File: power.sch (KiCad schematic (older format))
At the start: 50 parts, among them CN8 POWER, U1 68000D, U10 74LS244, U11 74LS373, U12 74LS244, U13 74LS373, U2 FAT_AGNUS_8375, U32 74LS139, U34 74LS373, U35 74LS244, U36 74LS05, U37 74LS32, U5 GARY_5719, X1 XTAL

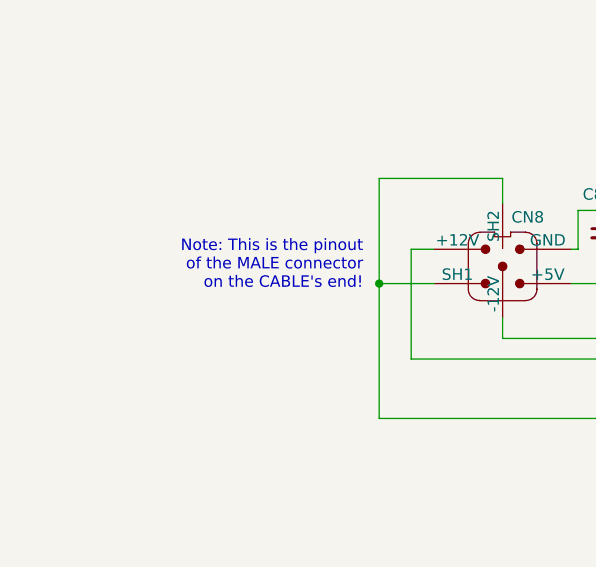
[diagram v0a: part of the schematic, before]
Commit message: Redo power connector and some cosmetic fixes here and there
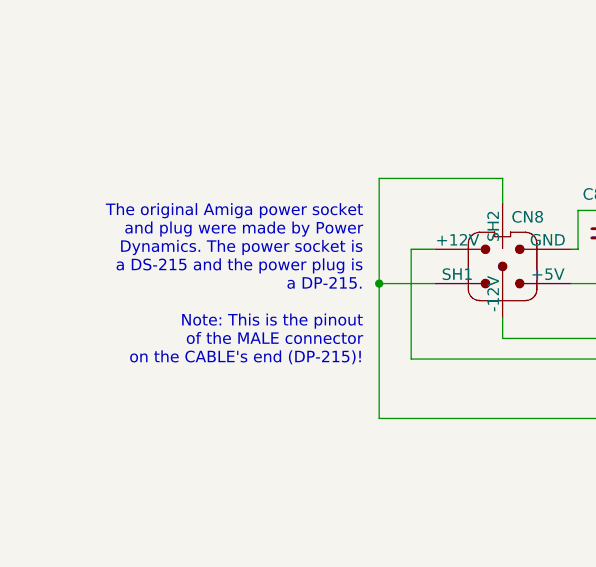
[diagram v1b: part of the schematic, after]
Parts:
- CN8: footprint Raemixx500:power_ami+din5 -> Raemixx500:DS215+DIN8_COMBO
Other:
- note added: "The original Amiga power socket\nand plug were made by Power\nDynamics. The power socket is\na DS-215 and the power plug is\na DP-215.\n\nNote: This is the pinout\nof the MALE connector\non the CABLE's end (DP-215)!"
- note removed: "Note: This is the pinout\nof the MALE connector\non the CABLE's end!"
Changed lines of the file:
@@
 F 0 "CN8" H 2930 2180 50  0000 C CNN
 F 1 "POWER" H 2680 2280 50  0001 C CNN
-F 2 "Raemixx500:power_ami+din5" H 870 2390 50  0001 C CNN
+F 2 "Raemixx500:DS215+DIN8_COMBO" H 870 2390 50  0001 C CNN
 F 3 "~" H 870 2390 50  0001 C CNN
 	1    2820 1940
@@
 	1    0    0    -1
 $EndComp
-Text Notes 2210 2020 2    50   ~ 0
-Note: This is the pinout\nof the MALE connector\non the CABLE's end!
+Text Notes 2210 2350 2    50   ~ 0
+The original Amiga power socket\nand plug were made by Power\nDynamics. The power socket is\na DS-215 and the power plug is\na DP-215.\n\nNote: This is the pinout\nof the MALE connector\non the CABLE's end (DP-215)!
 Wire Wire Line
 	3120 1990 3270 1990

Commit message: Begin adding part numbers
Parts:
- C1: Cost (none) -> 0.078; MFG Name (none) -> KEMET; MFG Part Num (none) -> C412C334M5U5TA; Optional (none) -> CPU
- C10, C12, C32, C34, C35, C36, C37, C701, C800, C801, C802, C803: Cost (none) -> 0.071; MFG Name (none) -> KEMET; MFG Part Num (none) -> C410C103K1H5TAAUTO
- C11, C13, C14, C5, C804: Cost (none) -> 0.078; MFG Name (none) -> KEMET; MFG Part Num (none) -> C412C334M5U5TA
- C2: Cost (none) -> 0.078; MFG Name (none) -> KEMET; MFG Part Num (none) -> C412C334M5U5TA; Optional (none) -> MEMORY
- CN8, LF1: Optional (none) -> POWER
- MT1, MT2, MT4, MT5, MT6, MT7: MFG Name (none) -> SKIP; MFG Part Num (none) -> SKIP; Optional (none) -> HOLE
- U1: Optional (none) -> CPU
- U10, U11, U12, U13, U32, U34, U35: Optional (none) -> MEMORY
- U2, U5: Optional (none) -> CUSTOM
- U36: Optional (none) -> FLOPPY/RTC
- U37: Optional (none) -> PARALLEL/FLOPPY/KEYBOARD
- X1: Optional (none) -> CLOCK

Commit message: More part numbers
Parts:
- C32, C34, C35: Optional (none) -> MEMORY
- C811, C812, C813, C814, C815, C816: Cost (none) -> 0.265; MFG Name (none) -> PANASONIC; MFG Part Num (none) -> EEUFR1H101
- MT1, MT2, MT4, MT5, MT6, MT7: Optional HOLE -> SKIP
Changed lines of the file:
@@
 F 5 "C410C103K1H5TAAUTO" H 2870 7060 50  0001 C CNN "MFG Part Num"
 F 6 "0.071" H 2870 7060 50  0001 C CNN "Cost"
+F 7 "MEMORY" H 2870 7060 50  0001 C CNN "Optional"
 	1    2870 7060
 	1    0    0    -1
@@
 F 5 "C410C103K1H5TAAUTO" H 4370 7060 50  0001 C CNN "MFG Part Num"
 F 6 "0.071" H 4370 7060 50  0001 C CNN "Cost"
+F 7 "MEMORY" H 4370 7060 50  0001 C CNN "Optional"
 	1    4370 7060
 	1    0    0    -1
@@
 F 5 "C410C103K1H5TAAUTO" H 5920 7060 50  0001 C CNN "MFG Part Num"
 F 6 "0.071" H 5920 7060 50  0001 C CNN "Cost"
+F 7 "MEMORY" H 5920 7060 50  0001 C CNN "Optional"
 	1    5920 7060
 	1    0    0    -1
@@
 F 2 "Capacitor_THT:CP_Radial_D8.0mm_P5.00mm" H 5590 2430 50  0001 C CNN
 F 3 "~" H 5590 2430 50  0001 C CNN
+F 4 "0.265" H 5590 2430 50  0001 C CNN "Cost"
+F 5 "PANASONIC" H 5590 2430 50  0001 C CNN "MFG Name"
+F 6 "EEUFR1H101" H 5590 2430 50  0001 C CNN "MFG Part Num"
 	1    5590 2430
 	1    0    0    -1
@@
 F 2 "Capacitor_THT:CP_Radial_D8.0mm_P5.00mm" H 6070 2430 50  0001 C CNN
 F 3 "~" H 6070 2430 50  0001 C CNN
+F 4 "0.265" H 6070 2430 50  0001 C CNN "Cost"
+F 5 "PANASONIC" H 6070 2430 50  0001 C CNN "MFG Name"
+F 6 "EEUFR1H101" H 6070 2430 50  0001 C CNN "MFG Part Num"
 	1    6070 2430
 	1    0    0    -1
@@
 F 2 "Capacitor_THT:CP_Radial_D8.0mm_P5.00mm" H 6550 2430 50  0001 C CNN
 F 3 "~" H 6550 2430 50  0001 C CNN
+F 4 "0.265" H 6550 2430 50  0001 C CNN "Cost"
+F 5 "PANASONIC" H 6550 2430 50  0001 C CNN "MFG Name"
+F 6 "EEUFR1H101" H 6550 2430 50  0001 C CNN "MFG Part Num"
 	1    6550 2430
 	1    0    0    -1
@@
 F 2 "Capacitor_THT:CP_Radial_D8.0mm_P5.00mm" H 7030 2430 50  0001 C CNN
 F 3 "~" H 7030 2430 50  0001 C CNN
+F 4 "0.265" H 7030 2430 50  0001 C CNN "Cost"
+F 5 "PANASONIC" H 7030 2430 50  0001 C CNN "MFG Name"
+F 6 "EEUFR1H101" H 7030 2430 50  0001 C CNN "MFG Part Num"
 	1    7030 2430
 	1    0    0    -1
@@
 F 2 "Capacitor_THT:CP_Radial_D8.0mm_P5.00mm" H 7510 2430 50  0001 C CNN
 F 3 "~" H 7510 2430 50  0001 C CNN
+F 4 "0.265" H 7510 2430 50  0001 C CNN "Cost"
+F 5 "PANASONIC" H 7510 2430 50  0001 C CNN "MFG Name"
+F 6 "EEUFR1H101" H 7510 2430 50  0001 C CNN "MFG Part Num"
 	1    7510 2430
 	1    0    0    -1
@@
 F 2 "Capacitor_THT:CP_Radial_D8.0mm_P5.00mm" H 7990 2430 50  0001 C CNN
 F 3 "~" H 7990 2430 50  0001 C CNN
+F 4 "0.265" H 7990 2430 50  0001 C CNN "Cost"
+F 5 "PANASONIC" H 7990 2430 50  0001 C CNN "MFG Name"
+F 6 "EEUFR1H101" H 7990 2430 50  0001 C CNN "MFG Part Num"
 	1    7990 2430
 	1    0    0    -1
@@
 F 4 "SKIP" H 8760 9250 50  0001 C CNN "MFG Name"
 F 5 "SKIP" H 8760 9250 50  0001 C CNN "MFG Part Num"
-F 6 "HOLE" H 8760 9250 50  0001 C CNN "Optional"
+F 6 "SKIP" H 8760 9250 50  0001 C CNN "Optional"
 	1    8760 9250
 	0    1    1    0
@@
 F 4 "SKIP" H 8760 9450 50  0001 C CNN "MFG Name"
 F 5 "SKIP" H 8760 9450 50  0001 C CNN "MFG Part Num"
-F 6 "HOLE" H 8760 9450 50  0001 C CNN "Optional"
+F 6 "SKIP" H 8760 9450 50  0001 C CNN "Optional"
 	1    8760 9450
 	0    1    1    0
@@
 F 4 "SKIP" H 8760 9650 50  0001 C CNN "MFG Name"
 F 5 "SKIP" H 8760 9650 50  0001 C CNN "MFG Part Num"
-F 6 "HOLE" H 8760 9650 50  0001 C CNN "Optional"
+F 6 "SKIP" H 8760 9650 50  0001 C CNN "Optional"
 	1    8760 9650
 	0    1    1    0
@@
 F 4 "SKIP" H 8760 9850 50  0001 C CNN "MFG Name"
 F 5 "SKIP" H 8760 9850 50  0001 C CNN "MFG Part Num"
-F 6 "HOLE" H 8760 9850 50  0001 C CNN "Optional"
+F 6 "SKIP" H 8760 9850 50  0001 C CNN "Optional"
 	1    8760 9850
 	0    1    1    0
@@
 F 4 "SKIP" H 8760 10050 50  0001 C CNN "MFG Name"
 F 5 "SKIP" H 8760 10050 50  0001 C CNN "MFG Part Num"
-F 6 "HOLE" H 8760 10050 50  0001 C CNN "Optional"
+F 6 "SKIP" H 8760 10050 50  0001 C CNN "Optional"
 	1    8760 10050
 	0    1    1    0
@@
 F 4 "SKIP" H 8760 10250 50  0001 C CNN "MFG Name"
 F 5 "SKIP" H 8760 10250 50  0001 C CNN "MFG Part Num"
-F 6 "HOLE" H 8760 10250 50  0001 C CNN "Optional"
+F 6 "SKIP" H 8760 10250 50  0001 C CNN "Optional"
 	1    8760 10250
 	0    1    1    0

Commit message: More part numbers
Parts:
- C821, C822: Cost (none) -> 0.137; MFG Name (none) -> PANASONIC; MFG Part Num (none) -> EEUFR1H470
- U10, U12, U35: Cost (none) -> 0.62; MFG Name (none) -> TI; MFG Part Num (none) -> SN74LS244N
- U11, U13, U34: Cost (none) -> 0.68; MFG Name (none) -> TI; MFG Part Num (none) -> SN74LS373N
- U32: Cost (none) -> 0.615; MFG Name (none) -> TI; MFG Part Num (none) -> SN74LS139AN
- U36: Cost (none) -> 0.668; MFG Name (none) -> TI; MFG Part Num (none) -> SN74LS05N
- U37: Cost (none) -> 0.442; MFG Name (none) -> TI; MFG Part Num (none) -> SN74LS32N
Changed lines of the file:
@@
 F 3 "http://www.ti.com/lit/gpn/sn74LS32" H 8570 7060 50  0001 C CNN
 F 4 "PARALLEL/FLOPPY/KEYBOARD" H 8570 7060 50  0001 C CNN "Optional"
+F 5 "0.442" H 8570 7060 50  0001 C CNN "Cost"
+F 6 "TI" H 8570 7060 50  0001 C CNN "MFG Name"
+F 7 "SN74LS32N" H 8570 7060 50  0001 C CNN "MFG Part Num"
 	5    8570 7060
 	1    0    0    -1
@@
 F 3 "http://www.ti.com/lit/gpn/sn74LS373" H 2870 9310 50  0001 C CNN
 F 4 "MEMORY" H 2870 9310 50  0001 C CNN "Optional"
+F 5 "0.68" H 2870 9310 50  0001 C CNN "Cost"
+F 6 "TI" H 2870 9310 50  0001 C CNN "MFG Name"
+F 7 "SN74LS373N" H 2870 9310 50  0001 C CNN "MFG Part Num"
 	2    2870 9310
 	1    0    0    -1
@@
 F 3 "http://www.ti.com/lit/gpn/sn74LS373" H 5720 9310 50  0001 C CNN
 F 4 "MEMORY" H 5720 9310 50  0001 C CNN "Optional"
+F 5 "0.68" H 5720 9310 50  0001 C CNN "Cost"
+F 6 "TI" H 5720 9310 50  0001 C CNN "MFG Name"
+F 7 "SN74LS373N" H 5720 9310 50  0001 C CNN "MFG Part Num"
 	2    5720 9310
 	1    0    0    -1
@@
 F 3 "http://www.ti.com/lit/gpn/sn74LS244" H 1370 9260 50  0001 C CNN
 F 4 "MEMORY" H 1370 9260 50  0001 C CNN "Optional"
+F 5 "0.62" H 1370 9260 50  0001 C CNN "Cost"
+F 6 "TI" H 1370 9260 50  0001 C CNN "MFG Name"
+F 7 "SN74LS244N" H 1370 9260 50  0001 C CNN "MFG Part Num"
 	2    1370 9260
 	1    0    0    -1
@@
 F 3 "http://www.ti.com/lit/gpn/sn74LS244" H 4220 9260 50  0001 C CNN
 F 4 "MEMORY" H 4220 9260 50  0001 C CNN "Optional"
+F 5 "0.62" H 4220 9260 50  0001 C CNN "Cost"
+F 6 "TI" H 4220 9260 50  0001 C CNN "MFG Name"
+F 7 "SN74LS244N" H 4220 9260 50  0001 C CNN "MFG Part Num"
 	2    4220 9260
 	1    0    0    -1
@@
 F 3 "http://www.ti.com/lit/gpn/sn74LS139" H 2320 7060 50  0001 C CNN
 F 4 "MEMORY" H 2320 7060 50  0001 C CNN "Optional"
+F 5 "0.615" H 2320 7060 50  0001 C CNN "Cost"
+F 6 "TI" H 2320 7060 50  0001 C CNN "MFG Name"
+F 7 "SN74LS139AN" H 2320 7060 50  0001 C CNN "MFG Part Num"
 	3    2320 7060
 	1    0    0    -1
@@
 F 3 "http://www.ti.com/lit/gpn/sn74LS373" H 3820 7110 50  0001 C CNN
 F 4 "MEMORY" H 3820 7110 50  0001 C CNN "Optional"
+F 5 "0.68" H 3820 7110 50  0001 C CNN "Cost"
+F 6 "TI" H 3820 7110 50  0001 C CNN "MFG Name"
+F 7 "SN74LS373N" H 3820 7110 50  0001 C CNN "MFG Part Num"
 	2    3820 7110
 	1    0    0    -1
@@
 F 3 "http://www.ti.com/lit/gpn/sn74LS244" H 5270 7060 50  0001 C CNN
 F 4 "MEMORY" H 5270 7060 50  0001 C CNN "Optional"
+F 5 "0.62" H 5270 7060 50  0001 C CNN "Cost"
+F 6 "TI" H 5270 7060 50  0001 C CNN "MFG Name"
+F 7 "SN74LS244N" H 5270 7060 50  0001 C CNN "MFG Part Num"
 	2    5270 7060
 	1    0    0    -1
@@
 F 3 "http://www.ti.com/lit/gpn/sn74LS05" H 6870 7060 50  0001 C CNN
 F 4 "FLOPPY/RTC" H 6870 7060 50  0001 C CNN "Optional"
+F 5 "0.668" H 6870 7060 50  0001 C CNN "Cost"
+F 6 "TI" H 6870 7060 50  0001 C CNN "MFG Name"
+F 7 "SN74LS05N" H 6870 7060 50  0001 C CNN "MFG Part Num"
 	7    6870 7060
 	1    0    0    -1
@@
 F 2 "Capacitor_THT:CP_Radial_D8.0mm_P5.00mm" H 5110 1620 50  0001 C CNN
 F 3 "~" H 5110 1620 50  0001 C CNN
+F 4 "0.137" H 5110 1620 50  0001 C CNN "Cost"
+F 5 "PANASONIC" H 5110 1620 50  0001 C CNN "MFG Name"
+F 6 "EEUFR1H470" H 5110 1620 50  0001 C CNN "MFG Part Num"
 	1    5110 1620
 	1    0    0    -1
@@
 F 2 "Capacitor_THT:CP_Radial_D8.0mm_P5.00mm" H 5110 1920 50  0001 C CNN
 F 3 "~" H 5110 1920 50  0001 C CNN
+F 4 "0.137" H 5110 1920 50  0001 C CNN "Cost"
+F 5 "PANASONIC" H 5110 1920 50  0001 C CNN "MFG Name"
+F 6 "EEUFR1H470" H 5110 1920 50  0001 C CNN "MFG Part Num"
 	1    5110 1920
 	1    0    0    -1

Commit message: Add EMI filter types
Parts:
- E101, E110: EMI_FILTER_TYPE (none) -> W/FERRITE
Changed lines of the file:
@@
 F 2 "Raemixx500:EMI_Filter_Short" V 4320 4110 50  0001 C CNN
 F 3 "http://www.murata.com/~/media/webrenewal/support/library/catalog/products/emc/emifil/c31e.ashx?la=en-gb" V 4320 4110 50  0001 C CNN
+F 4 "W/FERRITE" H 4320 4110 50  0001 C CNN "EMI_FILTER_TYPE"
 	1    4320 4110
 	0    1    1    0
@@
 F 2 "Raemixx500:EMI_Filter_Short" V 5770 4110 50  0001 C CNN
 F 3 "http://www.murata.com/~/media/webrenewal/support/library/catalog/products/emc/emifil/c31e.ashx?la=en-gb" V 5770 4110 50  0001 C CNN
+F 4 "W/FERRITE" H 5770 4110 50  0001 C CNN "EMI_FILTER_TYPE"
 	1    5770 4110
 	0    1    1    0

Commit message: Add part numbers for EMI filters Not the original filters, but what seem to be suitable replacements available today
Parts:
- E101, E110: Cost (none) -> 0.234; MFG Name (none) -> MURATA; MFG Part Num (none) -> DSS1NB32A151Q91A
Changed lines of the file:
@@
 F 3 "http://www.murata.com/~/media/webrenewal/support/library/catalog/products/emc/emifil/c31e.ashx?la=en-gb" V 4320 4110 50  0001 C CNN
 F 4 "W/FERRITE" H 4320 4110 50  0001 C CNN "EMI_FILTER_TYPE"
+F 5 "0.234" H 4320 4110 50  0001 C CNN "Cost"
+F 6 "MURATA" H 4320 4110 50  0001 C CNN "MFG Name"
+F 7 "DSS1NB32A151Q91A" H 4320 4110 50  0001 C CNN "MFG Part Num"
 	1    4320 4110
 	0    1    1    0
@@
 F 3 "http://www.murata.com/~/media/webrenewal/support/library/catalog/products/emc/emifil/c31e.ashx?la=en-gb" V 5770 4110 50  0001 C CNN
 F 4 "W/FERRITE" H 5770 4110 50  0001 C CNN "EMI_FILTER_TYPE"
+F 5 "0.234" H 5770 4110 50  0001 C CNN "Cost"
+F 6 "MURATA" H 5770 4110 50  0001 C CNN "MFG Name"
+F 7 "DSS1NB32A151Q91A" H 5770 4110 50  0001 C CNN "MFG Part Num"
 	1    5770 4110
 	0    1    1    0

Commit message: Add EMI filter 3D models, add logo, re-add Rock Lobster (closes #15) Thanks to Szabó Zoltán and Workshopshed!
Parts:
- E101, E110: MFG Part Num DSS1NB32A151Q91A -> DSS1NB32A103Q91A
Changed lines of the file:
@@
 F 5 "0.234" H 4320 4110 50  0001 C CNN "Cost"
 F 6 "MURATA" H 4320 4110 50  0001 C CNN "MFG Name"
-F 7 "DSS1NB32A151Q91A" H 4320 4110 50  0001 C CNN "MFG Part Num"
+F 7 "DSS1NB32A103Q91A" H 4320 4110 50  0001 C CNN "MFG Part Num"
 	1    4320 4110
 	0    1    1    0
@@
 F 5 "0.234" H 5770 4110 50  0001 C CNN "Cost"
 F 6 "MURATA" H 5770 4110 50  0001 C CNN "MFG Name"
-F 7 "DSS1NB32A151Q91A" H 5770 4110 50  0001 C CNN "MFG Part Num"
+F 7 "DSS1NB32A103Q91A" H 5770 4110 50  0001 C CNN "MFG Part Num"
 	1    5770 4110
 	0    1    1    0

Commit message: (Try to) Identify the minimum set of required components
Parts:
- C1, C10, C11, C12, C13, C2, C34, C35, C37, C5, C701, C800, C801, C804, C811, C812, C813, C814, C815, C816: Required (none) -> R
- CN8, E101, E110, LF1, U1, U10, U11, U12, U13, U2, U34, U35, U37, U5, X1: Required (none) -> Y
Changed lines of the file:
@@
 F 6 "TI" H 8570 7060 50  0001 C CNN "MFG Name"
 F 7 "SN74LS32N" H 8570 7060 50  0001 C CNN "MFG Part Num"
+F 8 "Y" H 8570 7060 50  0001 C CNN "Required"
 	5    8570 7060
 	1    0    0    -1
@@
 F 3 "DOCUMENTATION" H 7270 4810 50  0001 C CNN
 F 4 "CUSTOM" H 7270 5060 50  0001 C CNN "Optional"
+F 5 "Y" H 7270 5060 50  0001 C CNN "Required"
 	3    7270 5060
 	1    0    0    -1
@@
 F 3 "https://www.nxp.com/docs/en/reference-manual/MC68000UM.pdf" H 2920 5110 50  0001 C CNN
 F 4 "CPU" H 2920 5110 50  0001 C CNN "Optional"
+F 5 "Y" H 2920 5110 50  0001 C CNN "Required"
 	2    2920 5110
 	1    0    0    -1
@@
 F 3 "DOCUMENTATION" H 4320 5010 50  0001 C CNN
 F 4 "CUSTOM" H 4420 5010 50  0001 C CNN "Optional"
+F 5 "Y" H 4420 5010 50  0001 C CNN "Required"
 	2    4420 5010
 	1    0    0    -1
@@
 F 6 "0.078" H 3420 5060 50  0001 C CNN "Cost"
 F 7 "CPU" H 3420 5060 50  0001 C CNN "Optional"
+F 8 "R" H 3420 5060 50  0001 C CNN "Required"
 	1    3420 5060
 	1    0    0    -1
@@
 F 6 "MURATA" H 4320 4110 50  0001 C CNN "MFG Name"
 F 7 "DSS1NB32A103Q91A" H 4320 4110 50  0001 C CNN "MFG Part Num"
+F 8 "Y" H 4320 4110 50  0001 C CNN "Required"
 	1    4320 4110
 	0    1    1    0
@@
 F 6 "0.078" H 4820 5060 50  0001 C CNN "Cost"
 F 7 "MEMORY" H 4820 5060 50  0001 C CNN "Optional"
+F 8 "R" H 4820 5060 50  0001 C CNN "Required"
 	1    4820 5060
 	1    0    0    -1
@@
 F 6 "MURATA" H 5770 4110 50  0001 C CNN "MFG Name"
 F 7 "DSS1NB32A103Q91A" H 5770 4110 50  0001 C CNN "MFG Part Num"
+F 8 "Y" H 5770 4110 50  0001 C CNN "Required"
 	1    5770 4110
 	0    1    1    0
@@
 F 5 "C410C103K1H5TAAUTO" H 6270 5110 50  0001 C CNN "MFG Part Num"
 F 6 "0.071" H 6270 5110 50  0001 C CNN "Cost"
+F 7 "R" H 6270 5110 50  0001 C CNN "Required"
 	1    6270 5110
 	1    0    0    -1
@@
 F 5 "C412C334M5U5TA" H 8020 5110 50  0001 C CNN "MFG Part Num"
 F 6 "0.078" H 8020 5110 50  0001 C CNN "Cost"
+F 7 "R" H 8020 5110 50  0001 C CNN "Required"
 	1    8020 5110
 	1    0    0    -1
@@
 F 6 "TI" H 2870 9310 50  0001 C CNN "MFG Name"
 F 7 "SN74LS373N" H 2870 9310 50  0001 C CNN "MFG Part Num"
+F 8 "Y" H 2870 9310 50  0001 C CNN "Required"
 	2    2870 9310
 	1    0    0    -1
@@
 F 6 "TI" H 5720 9310 50  0001 C CNN "MFG Name"
 F 7 "SN74LS373N" H 5720 9310 50  0001 C CNN "MFG Part Num"
+F 8 "Y" H 5720 9310 50  0001 C CNN "Required"
 	2    5720 9310
 	1    0    0    -1
@@
 F 6 "TI" H 1370 9260 50  0001 C CNN "MFG Name"
 F 7 "SN74LS244N" H 1370 9260 50  0001 C CNN "MFG Part Num"
+F 8 "Y" H 1370 9260 50  0001 C CNN "Required"
 	2    1370 9260
 	1    0    0    -1
@@
 F 6 "TI" H 4220 9260 50  0001 C CNN "MFG Name"
 F 7 "SN74LS244N" H 4220 9260 50  0001 C CNN "MFG Part Num"
+F 8 "Y" H 4220 9260 50  0001 C CNN "Required"
 	2    4220 9260
 	1    0    0    -1
@@
 F 5 "C412C334M5U5TA" H 3470 9260 50  0001 C CNN "MFG Part Num"
 F 6 "0.078" H 3470 9260 50  0001 C CNN "Cost"
+F 7 "R" H 3470 9260 50  0001 C CNN "Required"
 	1    3470 9260
 	1    0    0    -1
@@
 F 5 "C412C334M5U5TA" H 6270 9260 50  0001 C CNN "MFG Part Num"
 F 6 "0.078" H 6270 9260 50  0001 C CNN "Cost"
+F 7 "R" H 6270 9260 50  0001 C CNN "Required"
 	1    6270 9260
 	1    0    0    -1
@@
 F 5 "C410C103K1H5TAAUTO" H 1920 9260 50  0001 C CNN "MFG Part Num"
 F 6 "0.071" H 1920 9260 50  0001 C CNN "Cost"
+F 7 "R" H 1920 9260 50  0001 C CNN "Required"
 	1    1920 9260
 	1    0    0    -1
@@
 F 5 "C410C103K1H5TAAUTO" H 4770 9260 50  0001 C CNN "MFG Part Num"
 F 6 "0.071" H 4770 9260 50  0001 C CNN "Cost"
+F 7 "R" H 4770 9260 50  0001 C CNN "Required"
 	1    4770 9260
 	1    0    0    -1
@@
 F 6 "TI" H 3820 7110 50  0001 C CNN "MFG Name"
 F 7 "SN74LS373N" H 3820 7110 50  0001 C CNN "MFG Part Num"
+F 8 "Y" H 3820 7110 50  0001 C CNN "Required"
 	2    3820 7110
 	1    0    0    -1
@@
 F 6 "TI" H 5270 7060 50  0001 C CNN "MFG Name"
 F 7 "SN74LS244N" H 5270 7060 50  0001 C CNN "MFG Part Num"
+F 8 "Y" H 5270 7060 50  0001 C CNN "Required"
 	2    5270 7060
 	1    0    0    -1
@@
 F 6 "0.071" H 4370 7060 50  0001 C CNN "Cost"
 F 7 "MEMORY" H 4370 7060 50  0001 C CNN "Optional"
+F 8 "R" H 4370 7060 50  0001 C CNN "Required"
 	1    4370 7060
 	1    0    0    -1
@@
 F 6 "0.071" H 5920 7060 50  0001 C CNN "Cost"
 F 7 "MEMORY" H 5920 7060 50  0001 C CNN "Optional"
+F 8 "R" H 5920 7060 50  0001 C CNN "Required"
 	1    5920 7060
 	1    0    0    -1
@@
 F 5 "C410C103K1H5TAAUTO" H 9370 7060 50  0001 C CNN "MFG Part Num"
 F 6 "0.071" H 9370 7060 50  0001 C CNN "Cost"
+F 7 "R" H 9370 7060 50  0001 C CNN "Required"
 	1    9370 7060
 	1    0    0    -1
@@
 F 3 "http://www.txccorp.com/download/products/osc/7C_o.pdf" H 5770 5010 50  0001 C CNN
 F 4 "CLOCK" H 5870 5010 50  0001 C CNN "Optional"
+F 5 "Y" H 5870 5010 50  0001 C CNN "Required"
 	2    5870 5010
 	1    0    0    -1
@@
 F 3 "~" H 870 2390 50  0001 C CNN
 F 4 "POWER" H 2820 1940 50  0001 C CNN "Optional"
+F 5 "Y" H 2820 1940 50  0001 C CNN "Required"
 	1    2820 1940
 	1    0    0    -1
@@
 F 3 "~" V 3690 1970 50  0001 C CNN
 F 4 "POWER" H 3690 1920 50  0001 C CNN "Optional"
+F 5 "Y" H 3690 1920 50  0001 C CNN "Required"
 	1    3690 1920
 	1    0    0    -1
@@
 F 5 "C410C103K1H5TAAUTO" H 4630 2430 50  0001 C CNN "MFG Part Num"
 F 6 "0.071" H 4630 2430 50  0001 C CNN "Cost"
+F 7 "R" H 4630 2430 50  0001 C CNN "Required"
 	1    4630 2430
 	1    0    0    -1
@@
 F 5 "C412C334M5U5TA" H 5110 2430 50  0001 C CNN "MFG Part Num"
 F 6 "0.078" H 5110 2430 50  0001 C CNN "Cost"
+F 7 "R" H 5110 2430 50  0001 C CNN "Required"
 	1    5110 2430
 	1    0    0    -1
@@
 F 5 "PANASONIC" H 5590 2430 50  0001 C CNN "MFG Name"
 F 6 "EEUFR1H101" H 5590 2430 50  0001 C CNN "MFG Part Num"
+F 7 "R" H 5590 2430 50  0001 C CNN "Required"
 	1    5590 2430
 	1    0    0    -1
@@
 F 5 "PANASONIC" H 6070 2430 50  0001 C CNN "MFG Name"
 F 6 "EEUFR1H101" H 6070 2430 50  0001 C CNN "MFG Part Num"
+F 7 "R" H 6070 2430 50  0001 C CNN "Required"
 	1    6070 2430
 	1    0    0    -1
@@
 F 5 "PANASONIC" H 6550 2430 50  0001 C CNN "MFG Name"
 F 6 "EEUFR1H101" H 6550 2430 50  0001 C CNN "MFG Part Num"
+F 7 "R" H 6550 2430 50  0001 C CNN "Required"
 	1    6550 2430
 	1    0    0    -1
@@
 F 5 "PANASONIC" H 7030 2430 50  0001 C CNN "MFG Name"
 F 6 "EEUFR1H101" H 7030 2430 50  0001 C CNN "MFG Part Num"
+F 7 "R" H 7030 2430 50  0001 C CNN "Required"
 	1    7030 2430
 	1    0    0    -1
@@
 F 5 "PANASONIC" H 7510 2430 50  0001 C CNN "MFG Name"
 F 6 "EEUFR1H101" H 7510 2430 50  0001 C CNN "MFG Part Num"
+F 7 "R" H 7510 2430 50  0001 C CNN "Required"
 	1    7510 2430
 	1    0    0    -1
@@
 F 5 "PANASONIC" H 7990 2430 50  0001 C CNN "MFG Name"
 F 6 "EEUFR1H101" H 7990 2430 50  0001 C CNN "MFG Part Num"
+F 7 "R" H 7990 2430 50  0001 C CNN "Required"
 	1    7990 2430
 	1    0    0    -1
@@
 F 5 "C410C103K1H5TAAUTO" H 3270 1770 50  0001 C CNN "MFG Part Num"
 F 6 "0.071" H 3270 1770 50  0001 C CNN "Cost"
+F 7 "R" H 3270 1770 50  0001 C CNN "Required"
 	1    3270 1770
 	1    0    0    -1
